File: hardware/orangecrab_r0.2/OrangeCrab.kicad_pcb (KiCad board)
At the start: 6 copper layers, 50.8 x 22.9 mm, 167 parts, among them J1 Conn_01x12_Male, J2 Conn_01x16_Male, J3 USB_B_Micro, J4 MicroSd, J5 JST, J6 JTAG, J7 Conn_02x15_Odd_Even, SW1 SW_Push, U1 FAN53541, U10 NCP115-2.5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

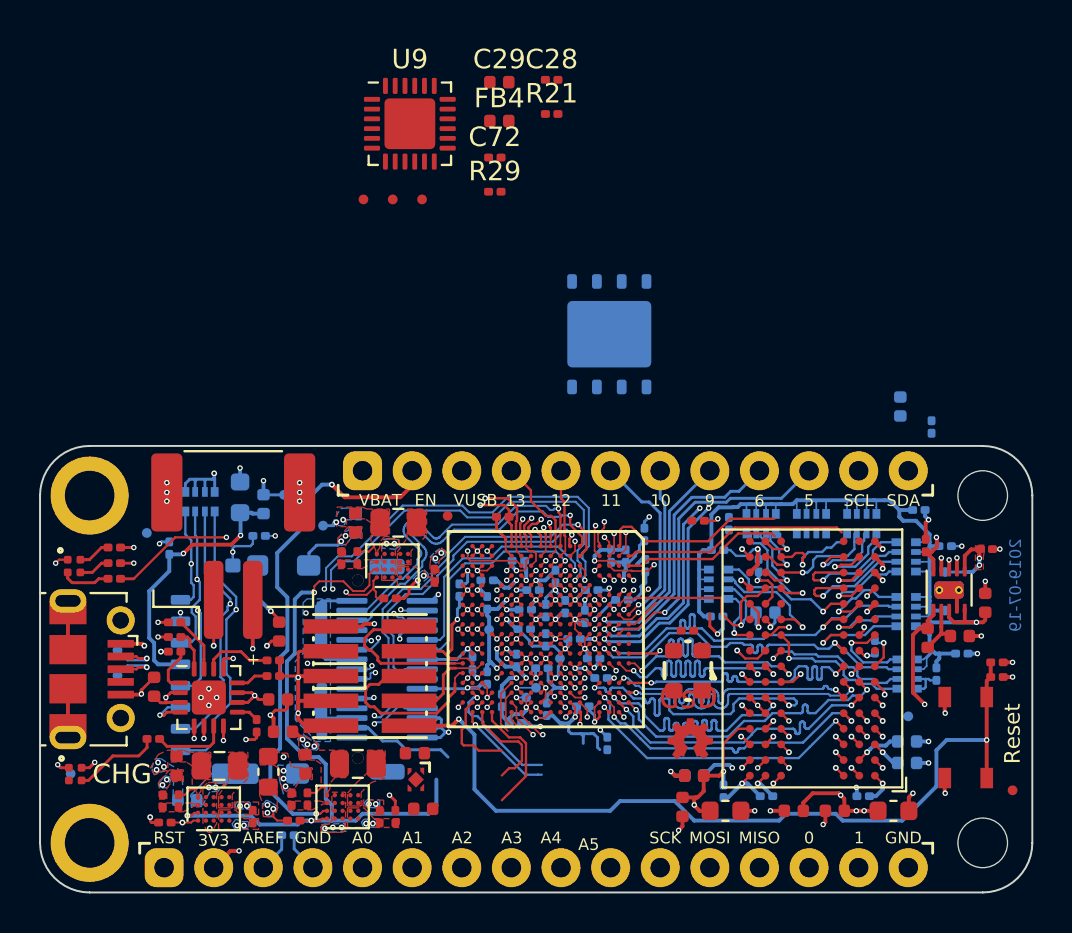
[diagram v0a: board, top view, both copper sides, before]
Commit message: hw: Update I/O block routing new DDR3 signals.
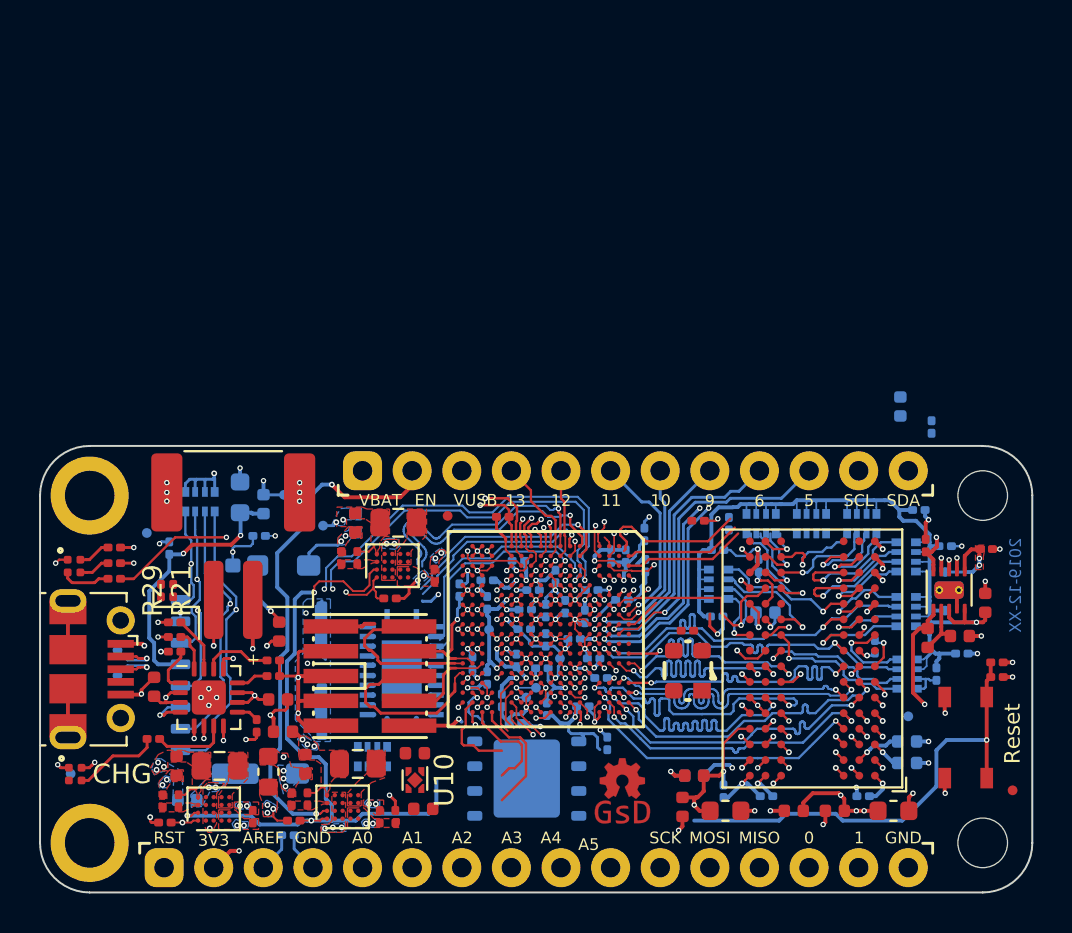
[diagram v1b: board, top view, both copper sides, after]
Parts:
- removed C28, C72: 100nF, Capacitor_SMD:C_0201_0603Metric
- removed C29: 4.7uF, Capacitor_SMD:C_0402_1005Metric
- removed FB4: 600R, Inductor_SMD:L_0402_1005Metric
- removed J7: Conn_02x15_Odd_Even, gkl_conn:DF12(3.0)-30DP-0.5V(86)
- removed the REF** at (163.7, 85.8)
- removed TP1, TP2, TP3: SMD_TP, gkl_misc:TestPoint_Pad_D0.5mm
- added RN9: 10k, Resistor_SMD:R_Array_Convex_4x0402, B.Cu at (151.5, 107.4)
- added U6: AT25SF081, Package_SON:WSON-8-1EP_6x5mm_P1.27mm_EP3.4x4mm, B.Cu at (159.4, 108.5)
- C76: value 100nF -> 10nF
- R21: value 4.7K -> 20R
- R29: value 1K -> 20R
- U10: footprint gkl_housings_son:X2SON_4_1.0x1.0mm -> Package_SON:Texas_X2SON-4_1x1mm_P0.65mm
- U9: value ATSAMD11D14A -> CD74HC4067M; footprint Package_DFN_QFN:QFN-24-1EP_4x4mm_P0.5mm_EP2.6x2.6mm -> Package_DFN_QFN:Texas_RGY_R-PVQFN-N24_EP2.05x3.1mm; moved to B.Cu
- moved R21 31.5 mm to (140.7, 98.9), turned to 270 degrees
- moved U9 28.0 mm to (153.0, 103.0)
- moved R29 26.2 mm to (141.3, 98.9), turned to 90 degrees
- moved G*** 6.80 mm to (164.3, 110.3)
- moved G*** 4.04 mm to (164.3, 108.6)
- moved U10 0.06 mm to (153.7, 108.6)
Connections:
- net Net-(U9-Pad21) renamed P1.2V
- C76 pad 1: FPGA_RESET -> USER_BUTTON
- J3 pad 2: USB_D- -> Net-(J3-Pad2)
- J3 pad 3: USB_D+ -> Net-(J3-Pad3)
- R20 pad 1: USB_D+ -> Net-(J3-Pad3)
- R21 pad 1: RESET -> Net-(J3-Pad3)
- R21 pad 2: Net-(C28-Pad1) -> USB_D+
- R29 pad 1: SWCLK -> USB_D-
- R29 pad 2: Net-(C28-Pad1) -> Net-(J3-Pad2)
- R4 pad 2: FPGA_RESET -> USER_BUTTON
- SW1 pad 2: FPGA_RESET -> USER_BUTTON
- U3 pad A13: RAM_D15 -> RAM_D7
- U3 pad A15: RAM_D12 -> RAM_D4
- U3 pad A17: RAM_D14 -> RAM_D6
- U3 pad B13: RAM_D13 -> RAM_D5
- U3 pad B17: RAM_D10 -> RAM_D2
- U3 pad C16: RAM_D11 -> RAM_D3
- U3 pad C17: RAM_D8 -> RAM_D0
- U3 pad C18: RAM_D5 -> RAM_D13
- U3 pad D15: RAM_D9 -> RAM_D1
- U3 pad F1: AUX_3+ -> Net-(U3-PadF1)
- U3 pad F15: RAM_D3 -> RAM_D11
- U3 pad F16: RAM_D1 -> RAM_D9
- U3 pad F17: RAM_D0 -> RAM_D8
- U3 pad F18: RAM_D7 -> RAM_D15
- U3 pad F2: AUX_2+ -> Net-(U3-PadF2)
- U3 pad F3: AUX_6- -> ADC_CTRL1
- U3 pad F4: AUX_6+ -> ADC_CTRL0
- U3 pad G1: AUX_2- -> Net-(U3-PadG1)
- U3 pad G15: RAM_D2 -> RAM_D10
- U3 pad G3: AUX_1- -> ADC_MUX3
- U3 pad G4: AUX_5- -> ADC_MUX1
- U3 pad H1: AUX_3- -> Net-(U3-PadH1)
- U3 pad H16: RAM_D6 -> RAM_D14
- U3 pad H3: AUX_1+ -> ADC_MUX2
- U3 pad H4: AUX_5+ -> ADC_MUX0
- U3 pad J16: RAM_D4 -> RAM_D12
- U3 pad K4: AUX_4+ -> ADC_SENSE_HI
- U3 pad L4: AUX_4- -> ADC_SENSE_LO
- U3 pad M3: AUX_7 -> Net-(U3-PadM3)
- U3 pad N3: AUX_0- -> Net-(U3-PadN3)
- U3 pad N4: AUX_0+ -> Net-(U3-PadN4)
- U4 pad A2: RAM_D5 -> RAM_D13
- U4 pad A3: RAM_D7 -> RAM_D15
- U4 pad A7: RAM_D4 -> RAM_D12
- U4 pad B8: RAM_D6 -> RAM_D14
- U4 pad C2: RAM_D3 -> RAM_D11
- U4 pad C3: RAM_D1 -> RAM_D9
- U4 pad C8: RAM_D2 -> RAM_D10
- U4 pad D7: RAM_D0 -> RAM_D8
- U4 pad E3: RAM_D8 -> RAM_D0
- U4 pad F2: RAM_D10 -> RAM_D2
- U4 pad F7: RAM_D9 -> RAM_D1
- U4 pad F8: RAM_D11 -> RAM_D3
- U4 pad G2: RAM_D14 -> RAM_D6
- U4 pad H3: RAM_D12 -> RAM_D4
- U4 pad H7: RAM_D15 -> RAM_D7
- U4 pad H8: RAM_D13 -> RAM_D5
- U9 pad 1: /sheetIO/A2 -> Net-(RN9-Pad8)
- U9 pad 10: /sheetIO/A0 -> ADC_MUX0
- U9 pad 11: Net-(U9-Pad11) -> ADC_MUX1
- U9 pad 12: Net-(U9-Pad12) -> GND
- U9 pad 13: SPI_0 -> ADC_MUX3
- U9 pad 14: SPI_1 -> ADC_MUX2
- U9 pad 15: SPI_2 -> ADC_CTRL1
- U9 pad 16: SPI_3 -> Net-(U9-Pad16)
- U9 pad 18: RESET -> Net-(U9-Pad18)
- U9 pad 19: SWCLK -> Net-(U9-Pad19)
- U9 pad 2: /sheetIO/AREF -> P3.3V
- U9 pad 20: SWDIO -> Net-(U9-Pad20)
- U9 pad 22: Net-(U9-Pad22) -> P1.35V
- U9 pad 23: GND -> P2.5V
- U9 pad 24: Net-(C28-Pad1) -> P3.3V
- U9 pad 25: GND -> (no net)
- U9 pad 3: /sheetIO/A4 -> /sheetIO/A5
- U9 pad 4: /sheetIO/A5 -> /sheetIO/A4
- U9 pad 6: Net-(U9-Pad6) -> /sheetIO/A2
- U9 pad 7: Net-(U9-Pad7) -> /sheetIO/A1
- U9 pad 8: Net-(U9-Pad8) -> /sheetIO/A0
- U9 pad 9: /sheetIO/A1 -> GND
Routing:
- net FPGA_RESET: track 65.3 -> 25.2 mm, vias 3 -> 2
- net AUX_6-: track 33.0 -> 0.00 mm, vias 3 -> 0
- net AUX_6+: track 31.2 -> 0.00 mm, vias 3 -> 0
- net ADC_CTRL1: track 0.00 -> 30.1 mm, vias 0 -> 2
- net ADC_CTRL0: track 0.00 -> 28.3 mm, vias 0 -> 2
- net USER_BUTTON: track 0.00 -> 24.1 mm, vias 0 -> 1
- net AUX_2+: track 19.1 -> 0.00 mm, vias 1 -> 0
- net GND: track 207.3 -> 188.5 mm, vias 136 -> 134
- net AUX_3+: track 18.6 -> 0.00 mm, vias 1 -> 0
- net AUX_3-: track 17.8 -> 0.00 mm, vias 1 -> 0
- net AUX_2-: track 16.7 -> 0.00 mm, vias 1 -> 0
- net AUX_5-: track 16.3 -> 0.00 mm, vias 2 -> 0
- net AUX_7: track 15.9 -> 0.00 mm, vias 2 -> 0
- net AUX_5+: track 15.7 -> 0.00 mm, vias 2 -> 0
- net ADC_MUX1: track 0.00 -> 15.2 mm, vias 0 -> 1
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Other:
- board text added: "2019-12-XX"
- board text removed: "2019-07-19"

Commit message: hw: update DDR3 signals
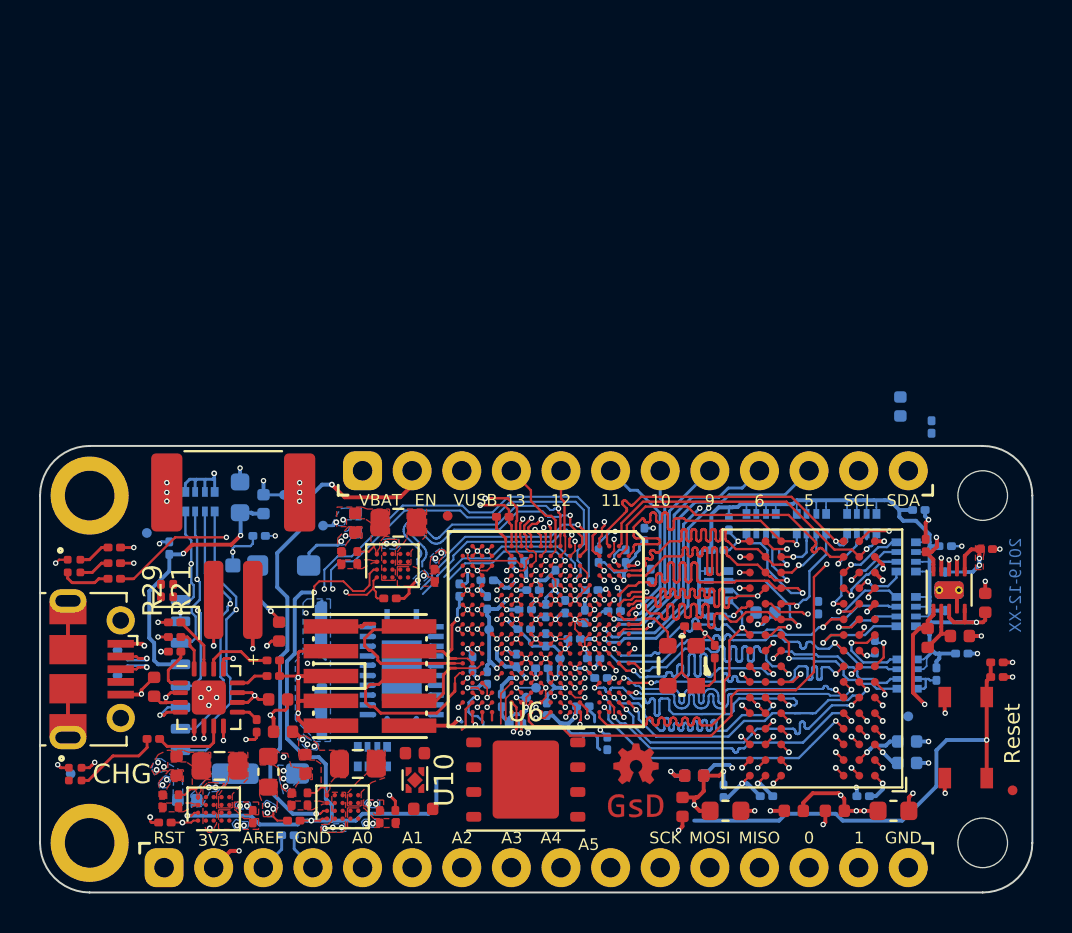
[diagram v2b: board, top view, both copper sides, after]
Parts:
- U6: moved to F.Cu
- moved C74 6.75 mm to (169.1, 102.0), turned to 90 degrees
- moved C44 3.73 mm to (174.4, 99.8)
- moved G*** 1.03 mm to (165.0, 107.8)
- moved G*** 0.75 mm to (165.0, 110.0)
- moved C59 0.70 mm to (163.9, 100.0)
- moved C1 0.65 mm to (163.1, 97.2)
- moved C62 0.57 mm to (165.8, 98.2)
- moved OSC1 0.39 mm to (167.4, 102.8)
- moved C75 0.29 mm to (167.8, 100.8)
- moved RN4 0.08 mm to (169.2, 98.7)
- moved U6 0.07 mm to (159.4, 108.6)
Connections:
- RN2 pad 7: RAM_A1 -> RAM_BA2
- RN2 pad 8: RAM_A11 -> RAM_A13
- RN4 pad 5: RAM_BA2 -> Net-(RN4-Pad5)
- RN8 pad 5: Net-(RN8-Pad5) -> RAM_A15
- RN8 pad 6: RAM_A15 -> RAM_A1
- RN8 pad 7: RAM_A14 -> RAM_A11
- RN8 pad 8: RAM_A13 -> RAM_A14
- U3 pad A2: RAM_A9 -> RAM_A14
- U3 pad A3: RAM_A13 -> RAM_A5
- U3 pad A4: RAM_A0 -> RAM_A4
- U3 pad B1: RAM_A14 -> RAM_A7
- U3 pad B2: RAM_A7 -> RAM_A9
- U3 pad B6: RAM_BA0 -> RAM_A12
- U3 pad C1: RAM_A8 -> RAM_A13
- U3 pad C3: RAM_A2 -> RAM_A6
- U3 pad C4: RAM_A12 -> RAM_A3
- U3 pad C7: RAM_A3 -> RAM_A15
- U3 pad D1: RAM_A6 -> RAM_A1
- U3 pad D18: P1.35V -> RAM_CKE
- U3 pad D2: RAM_A1 -> RAM_A8
- U3 pad D3: RAM_A4 -> RAM_A2
- U3 pad D4: RAM_A5 -> RAM_A0
- U3 pad D6: RAM_A15 -> RAM_BA0
- U3 pad K17: RAM_CKE -> P1.35V
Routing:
- net RAM_RESET#: track 0.00 -> 28.8 mm, vias 0 -> 2
- net RAM_A15: track 0.00 -> 19.7 mm, vias 0 -> 2
- net RAM_A8: track 2.77 -> 14.9 mm, vias 1 -> 2
- net RAM_A13: track 6.29 -> 16.6 mm, vias 0 -> 1
- net RAM_A14: track 7.77 -> 16.2 mm, vias 0 -> 1
- net RAM_A9: track 10.5 -> 17.2 mm
- net RAM_BA1: track 23.9 -> 17.2 mm
- net P3.3V: track 38.8 -> 45.0 mm, vias 18 -> 19
- net GND: track 188.5 -> 182.5 mm, vias 134 -> 135
- net QSPI_D2: track 6.08 -> 0.42 mm
- net SPI_CONFIG_MISO: track 5.20 -> 0.55 mm
- net RAM_BA2: track 21.2 -> 16.5 mm
- net VTT_REF: track 38.1 -> 33.7 mm
- net P1.35V: track 88.4 -> 84.1 mm, vias 15 -> 14
- net ADC_MUX2: track 10.9 -> 7.08 mm
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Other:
- net class DDR3_CTRL_LM1.0: clearance 0.089 -> 0.1524

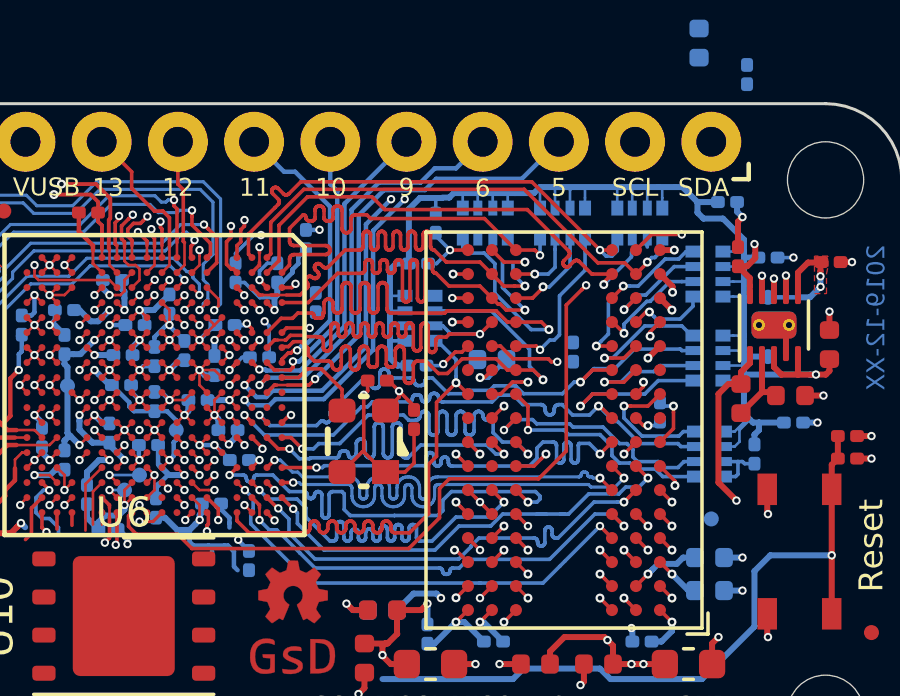
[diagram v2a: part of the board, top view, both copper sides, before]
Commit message: hw: Completed first pass of new DD3 routing.
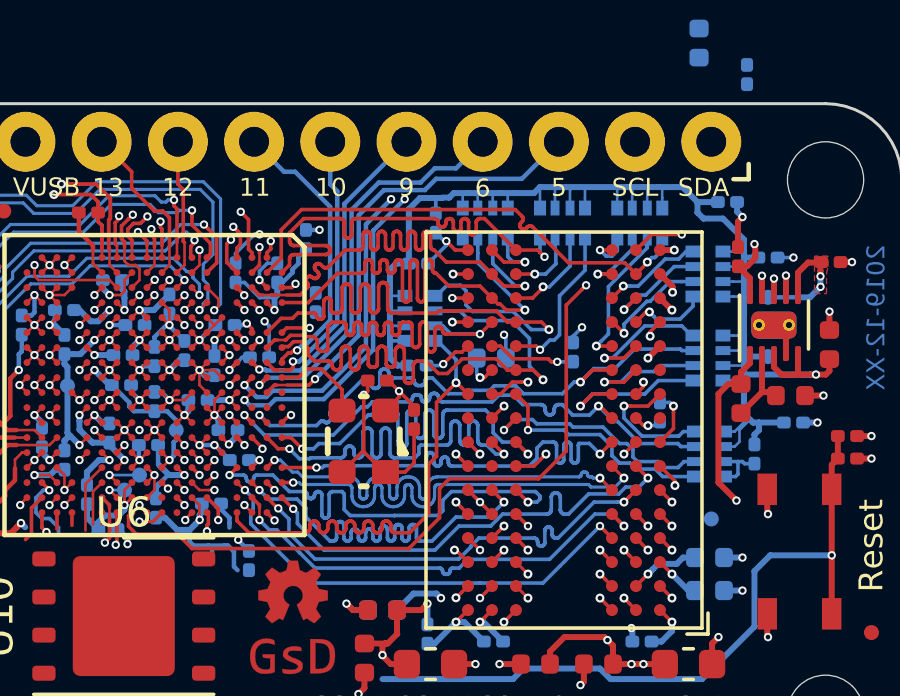
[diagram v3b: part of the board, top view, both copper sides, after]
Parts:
- moved R19 0.06 mm to (171.6, 100.0), turned to 0 degrees
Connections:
- RN1 pad 8: RAM_A12 -> Net-(RN1-Pad8)
- RN2 pad 6: RAM_A9 -> RAM_BA2
- RN2 pad 7: RAM_BA2 -> RAM_A9
- RN4 pad 5: Net-(RN4-Pad5) -> RAM_A12
- U3 pad A3: RAM_A5 -> RAM_A3
- U3 pad B1: RAM_A7 -> RAM_A8
- U3 pad B2: RAM_A9 -> RAM_A7
- U3 pad C4: RAM_A3 -> RAM_A0
- U3 pad D1: RAM_A1 -> RAM_A9
- U3 pad D2: RAM_A8 -> RAM_A1
- U3 pad D4: RAM_A0 -> RAM_A5
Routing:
- net RAM_BA2: track 16.5 -> 19.4 mm
- net /sheetHyperRAM/RAM_VDD: track 13.6 -> 15.6 mm
- net GND: track 182.5 -> 183.9 mm, vias 135 -> 137
- net RAM_D7: track 14.5 -> 15.9 mm
- net RAM_A8: track 14.9 -> 16.3 mm
- net RAM_D5: track 14.5 -> 15.9 mm
- net RAM_A6: track 17.4 -> 18.7 mm
- net RAM_A4: track 18.2 -> 19.3 mm
- net RAM_D6: track 15.1 -> 15.9 mm
- net RAM_CAS#: track 19.8 -> 19.1 mm
- net RAM_A11: track 17.5 -> 16.8 mm
- net RAM_A5: track 18.6 -> 18.0 mm
- net RAM_A3: track 17.6 -> 17.0 mm
- net RAM_BA1: track 17.2 -> 16.6 mm
- net RAM_A2: track 18.4 -> 17.9 mm
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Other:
- net class DDR3_CTRL_LM1.0: clearance 0.1524 -> 0.1778
- board text added: "r0.2"
- board text removed: "r0.1"
